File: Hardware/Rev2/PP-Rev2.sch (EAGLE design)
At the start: 181 parts, among them IC1 LT6004, IC2 TLC6C5912-Q1, J1 J_0399700102, Q1 MOSFET-PCHANNEL, Q10 2N7002PW, Q11 2N7002PW, Q12 2N7002PW, Q13 2N7002PW, Q14 2N7002PW, Q15 2N7002PW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

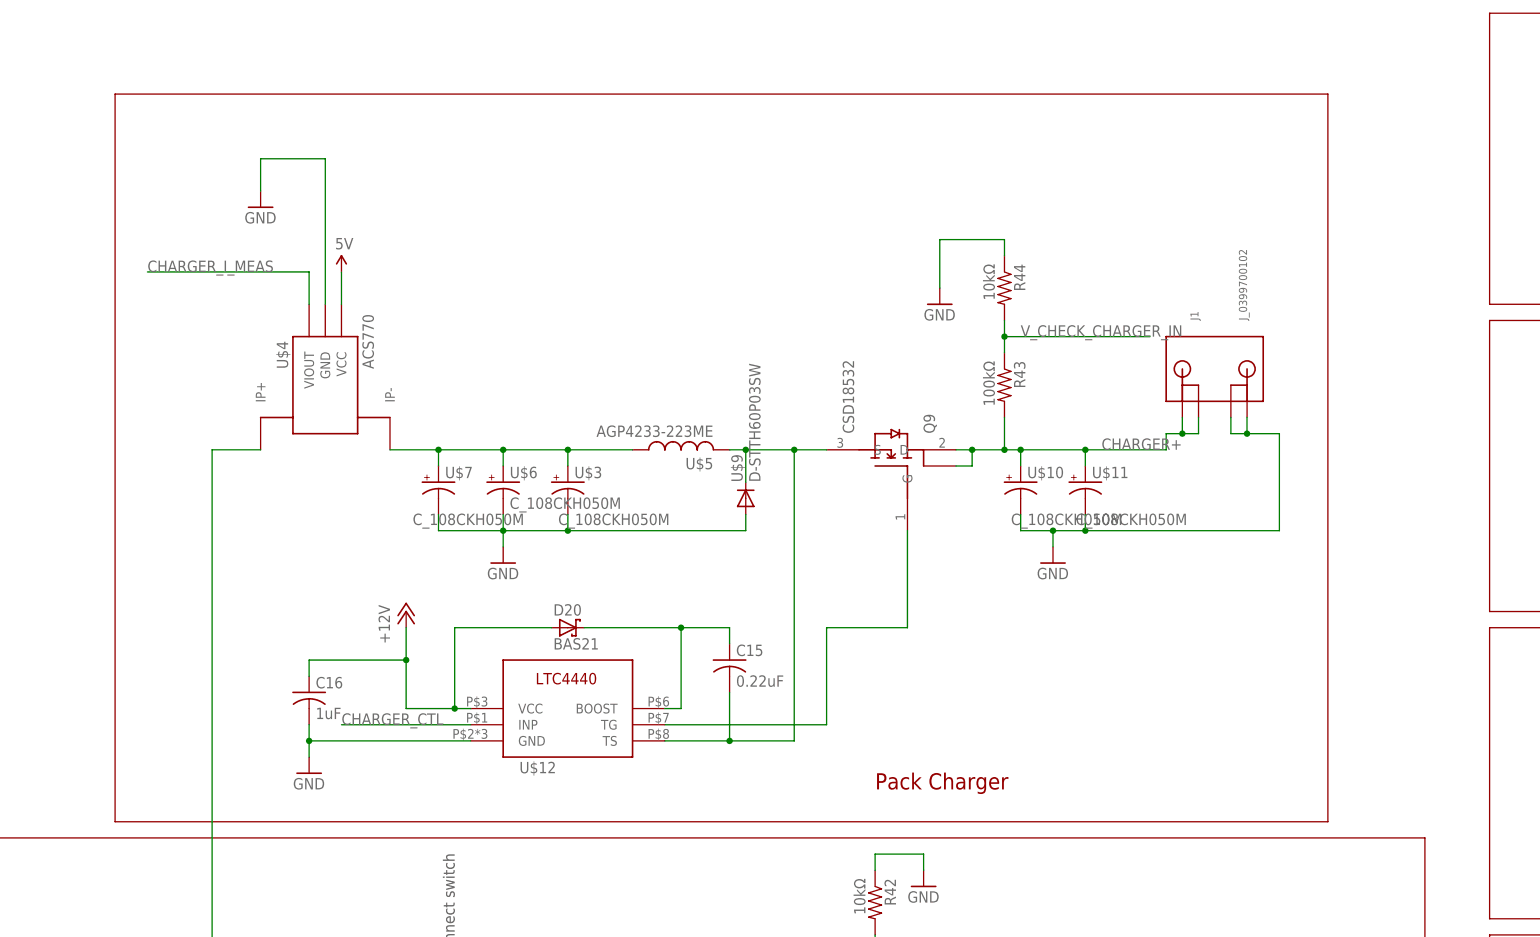
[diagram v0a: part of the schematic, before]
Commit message: Changing out charger MOSFET to proper component
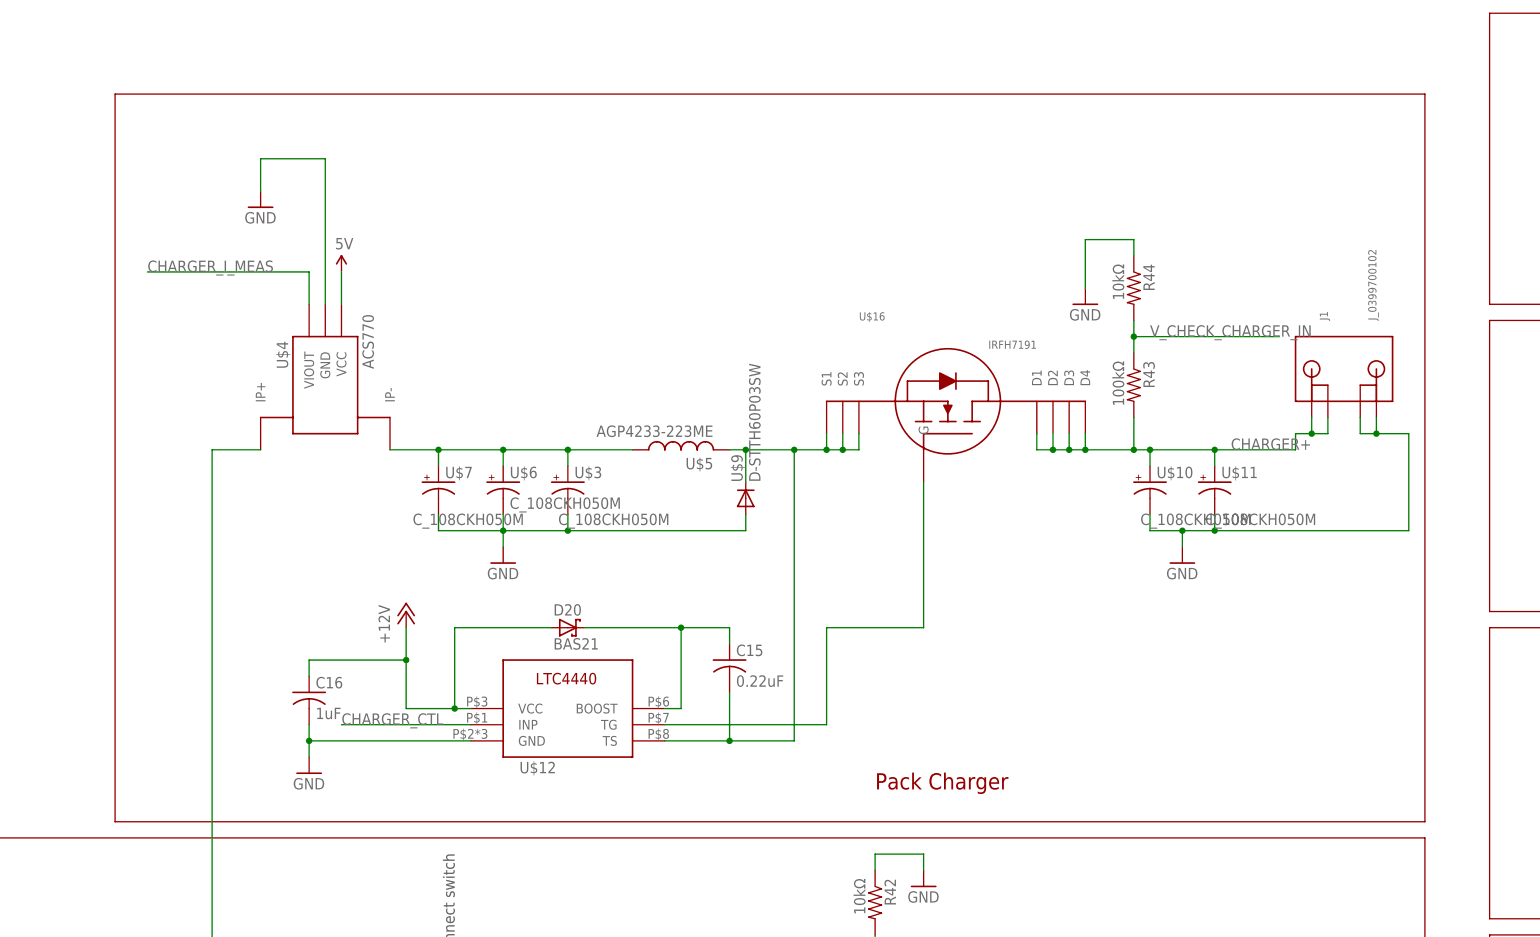
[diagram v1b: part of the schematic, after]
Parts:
- removed Q9: CSD18532, PCB0M1:Q_CSD18532KCSPCB
- added U$16: IRFH7191, 2016PowerPackLibraries:IRFH7191
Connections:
- net CHARGER+: now also U$16.D1, U$16.D2, U$16.D3, U$16.D4; no longer Q9.D, Q9.P$1
- net N$39: now also U$16.S1, U$16.S2, U$16.S3; no longer Q9.S
- net N$40: now also U$16.G; no longer Q9.G
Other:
- moved on the sheet: J1, R43, R44, U$10, U$11

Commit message: Reconfigure board and schematic to include second MOSFET to make synchronous switching possible on the buck converter
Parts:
- removed U$12: LTC4440, 2016PowerPackLibraries:LTC4440
- added U$17: IRFH7191, 2016PowerPackLibraries:IRFH7191
- added U$18: LTC4444, 2016PowerPackLibraries:LTC4444
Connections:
- removed net CHARGER_CTL: U$12.INP, U$13.P8.0
- new net CHARGER_CTL_B: U$13.P7.6, U$18.BINP
- new net CHARGER_CTL_T: U$13.P8.0, U$18.TINP
- new net N$65: U$17.G, U$18.BG
- net +12V: now also U$18.VCC; no longer U$12.VCC
- net GND: now also U$17.S1, U$17.S2, U$17.S3, U$18.GND; no longer U$12.GND
- net N$38: now also U$18.BOOST; no longer U$12.BOOST
- net N$39: now also U$17.D1, U$17.D2, U$17.D3, U$17.D4, U$18.TS; no longer U$12.TS
- net N$40: now also U$18.TG; no longer U$12.TG
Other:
- moved on the sheet: J1, R43, R44, U$10, U$11, U$16, U$3, U$4, U$5, U$6, U$7, U$9

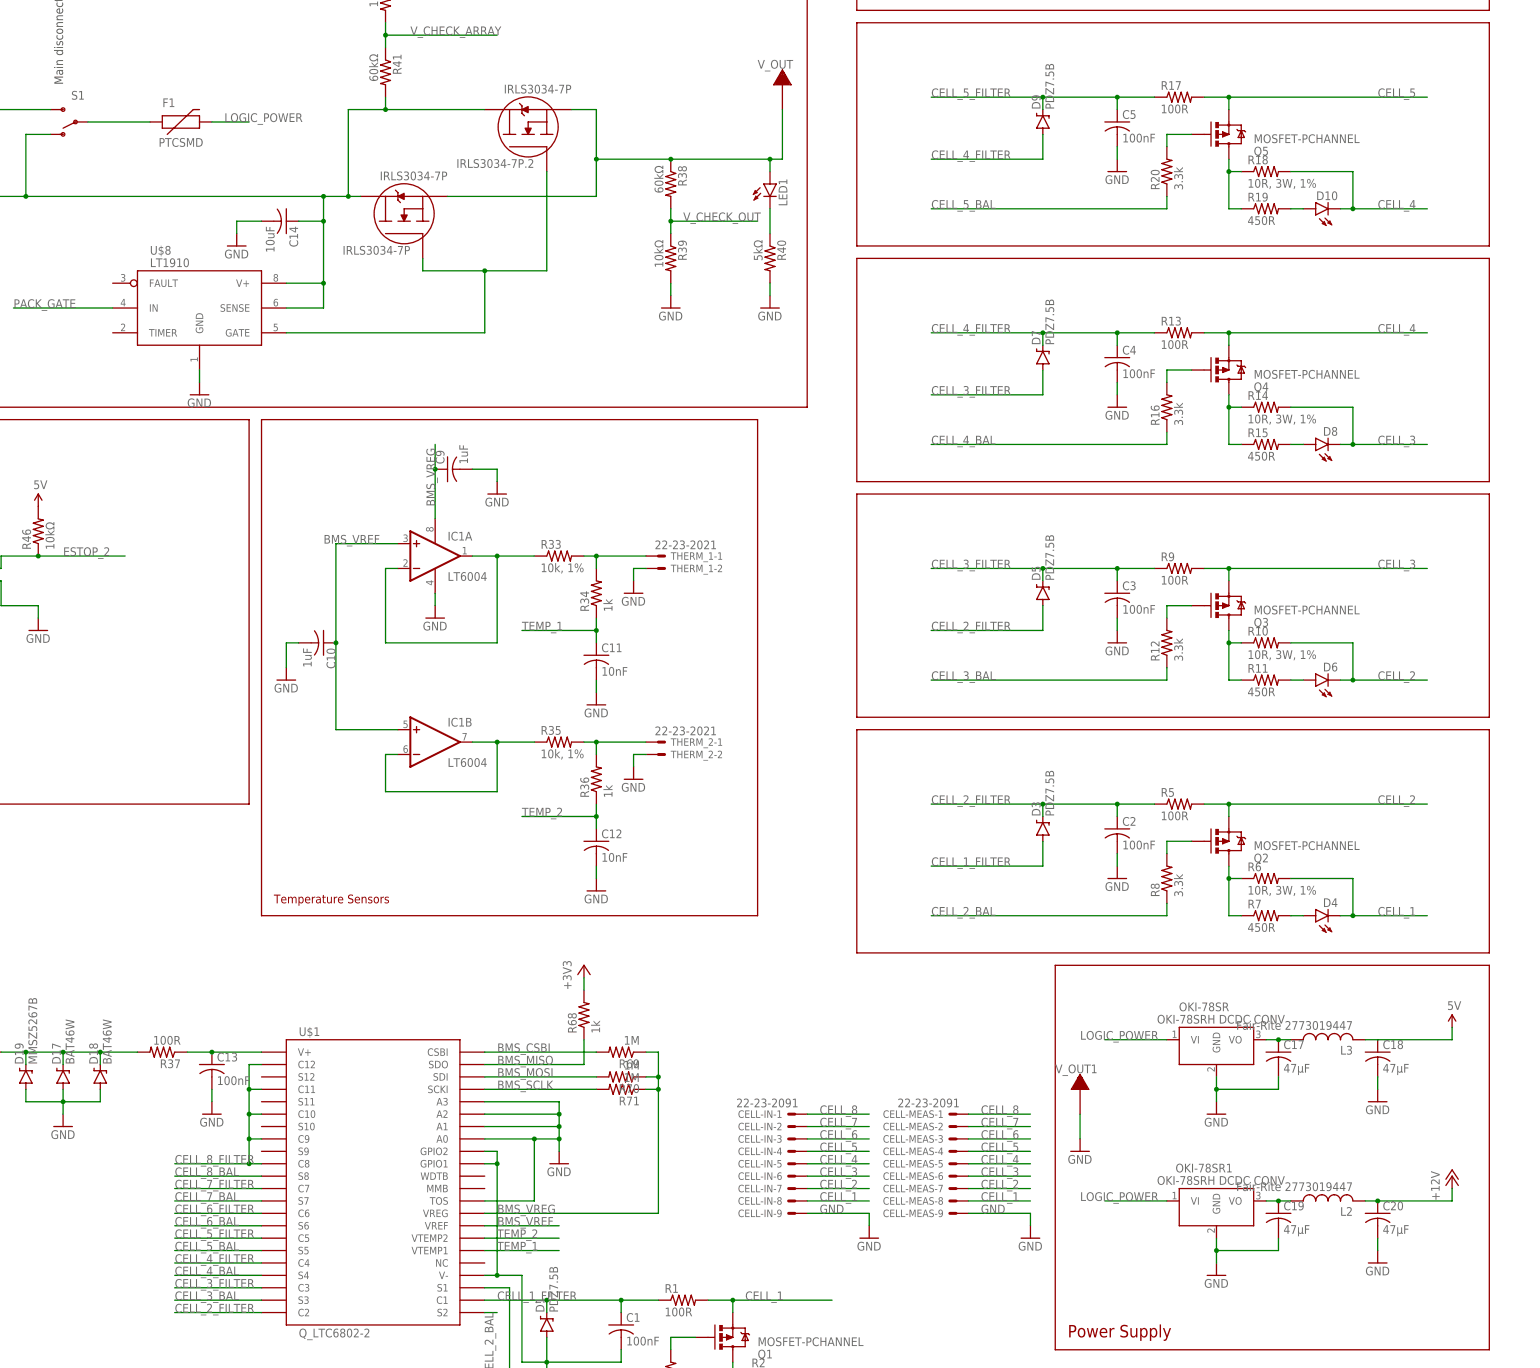
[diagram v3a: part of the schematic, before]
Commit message: Update board power supply to use proper input/output filtering caps, properly sized PTC fuse on input from battery pack
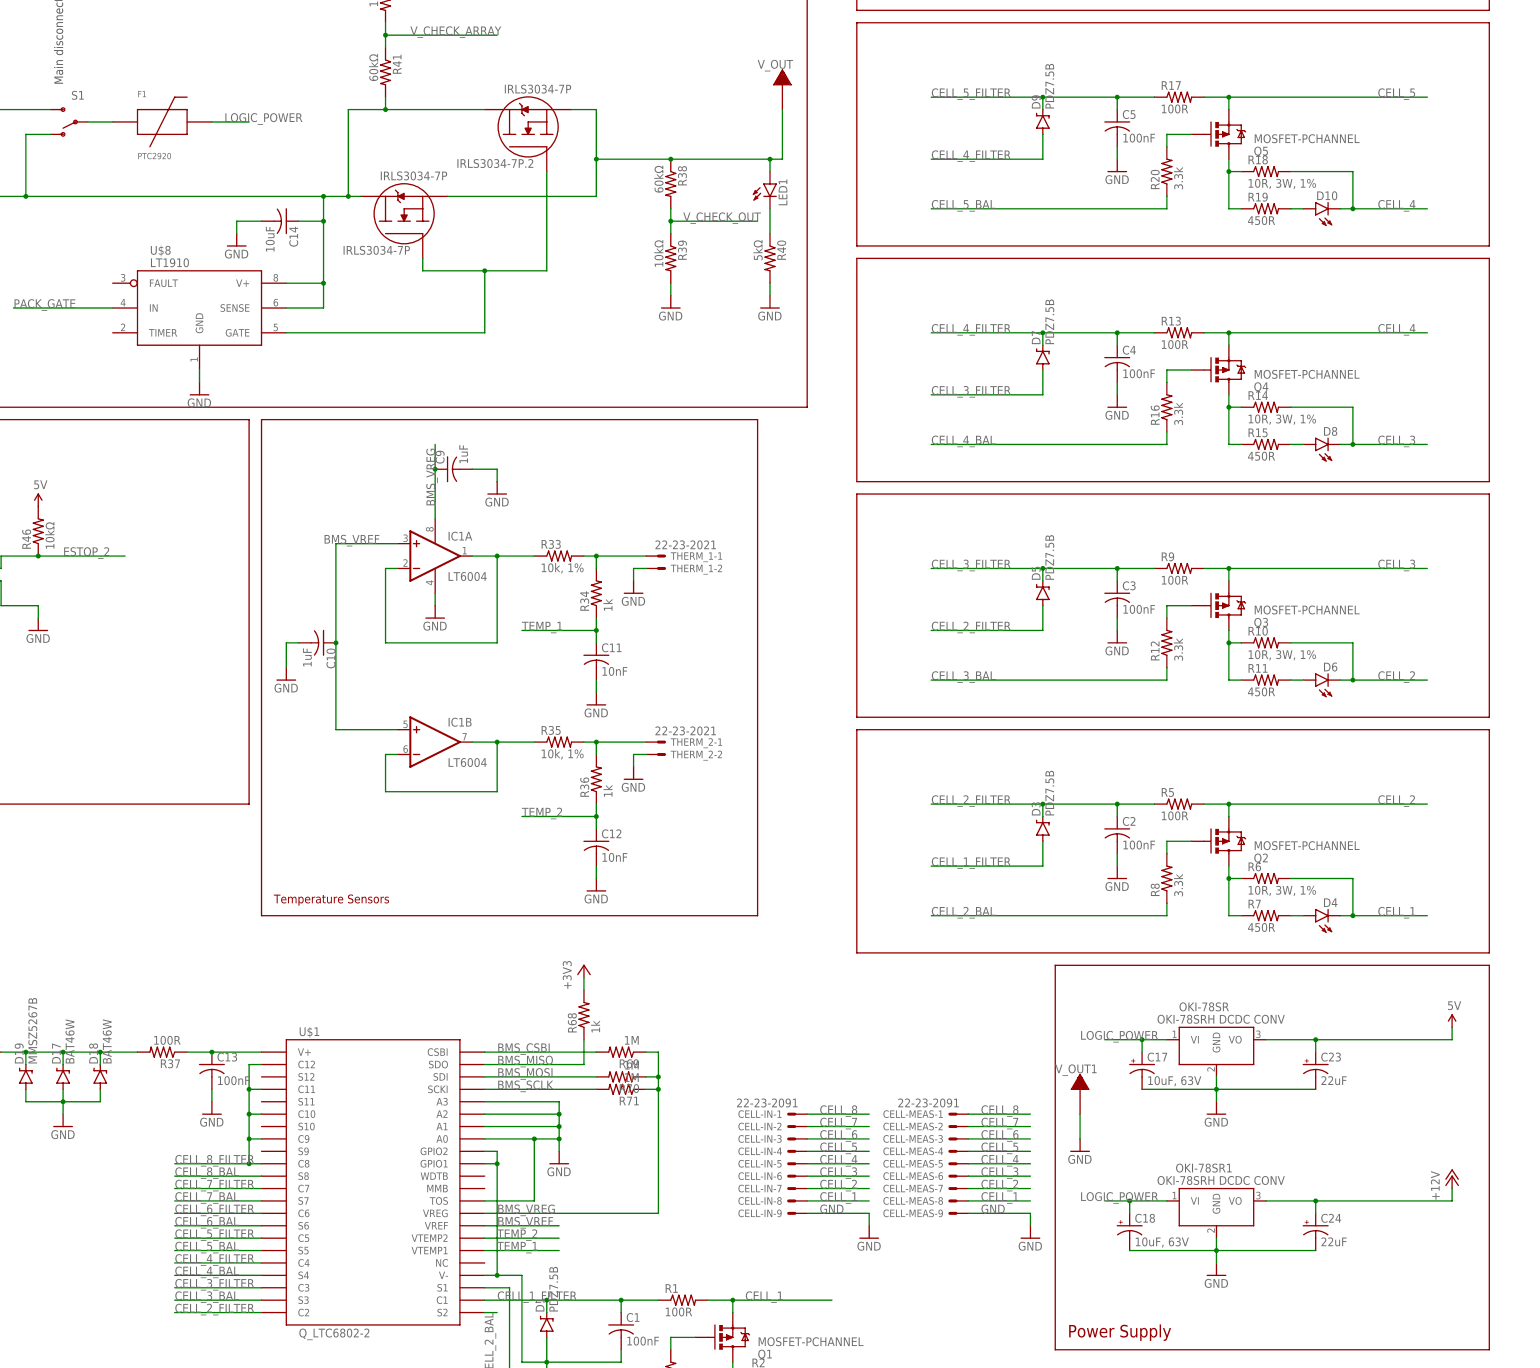
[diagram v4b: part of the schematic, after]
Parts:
- removed C19, C20: 47µF, resistor:C-USC1206
- removed L2, L3: Fair-Rite 2773019447, rcl:L-USL8530M
- added C23, C24: 22uF, rcl:CPOL-USD
- C17, C18: value 47µF -> 10uF, 63V; device resistor:C-USC1206 -> rcl:CPOL-USD
- F1: value PTCSMD -> PTC2920; device SparkFun-PowerIC:PTCSMD -> 2016PowerPackLibraries:PTC2920
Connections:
- removed net N$100: C17.1, L3.1, OKI-78SR.VO
- removed net N$33: C19.1, L2.1, OKI-78SR1.VO
- net +12V: now also C24.+, OKI-78SR1.VO; no longer C20.1, L2.2
- net 5V: now also C23.+, OKI-78SR.VO; no longer C18.1, L3.2
- net GND: now also C17.-, C18.-, C23.-, C24.-; no longer C17.2, C18.2, C19.2, C20.2
- net LOGIC_POWER: now also C17.+, C18.+, F1.P$2; no longer F1.2
- net N$42: now also F1.P$1; no longer F1.1
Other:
- moved on the sheet: F1
